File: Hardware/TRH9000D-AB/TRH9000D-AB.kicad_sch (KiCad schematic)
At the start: 22 parts, among them J5 DIN-8_SDF-80J, U4 74VHC138, U5 T.I_SN74LVC2G32DCTR, U8 LMH1980

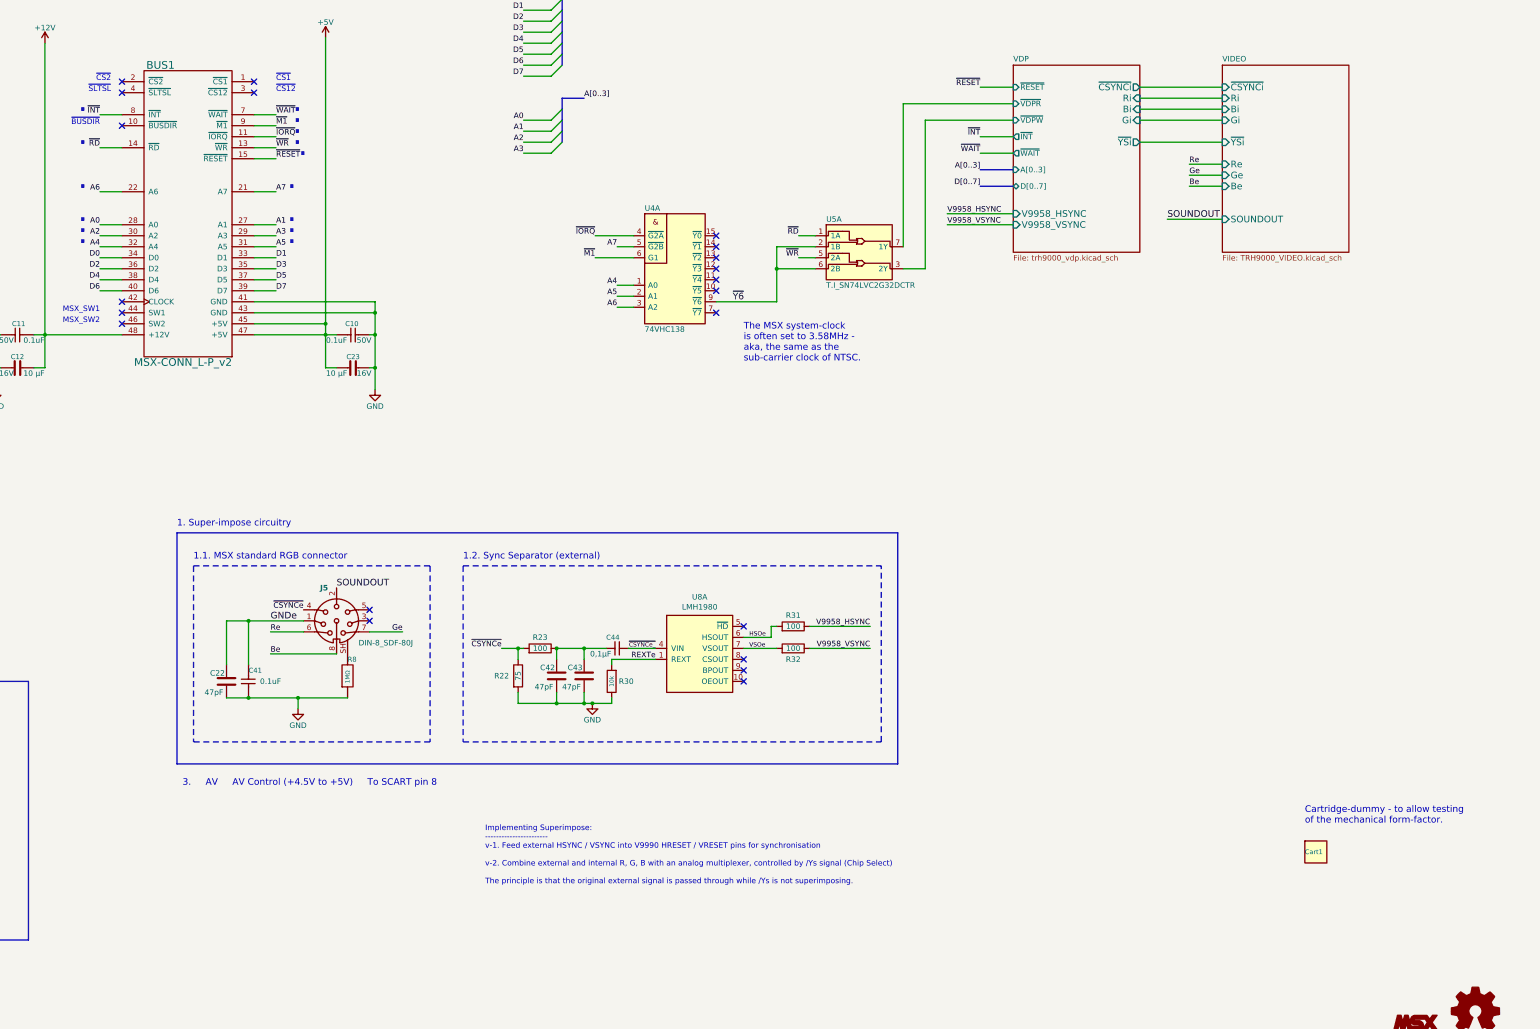
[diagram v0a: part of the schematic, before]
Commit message: Finished rerouting the AA-variant, and replaced the fuses with SMD-ones.
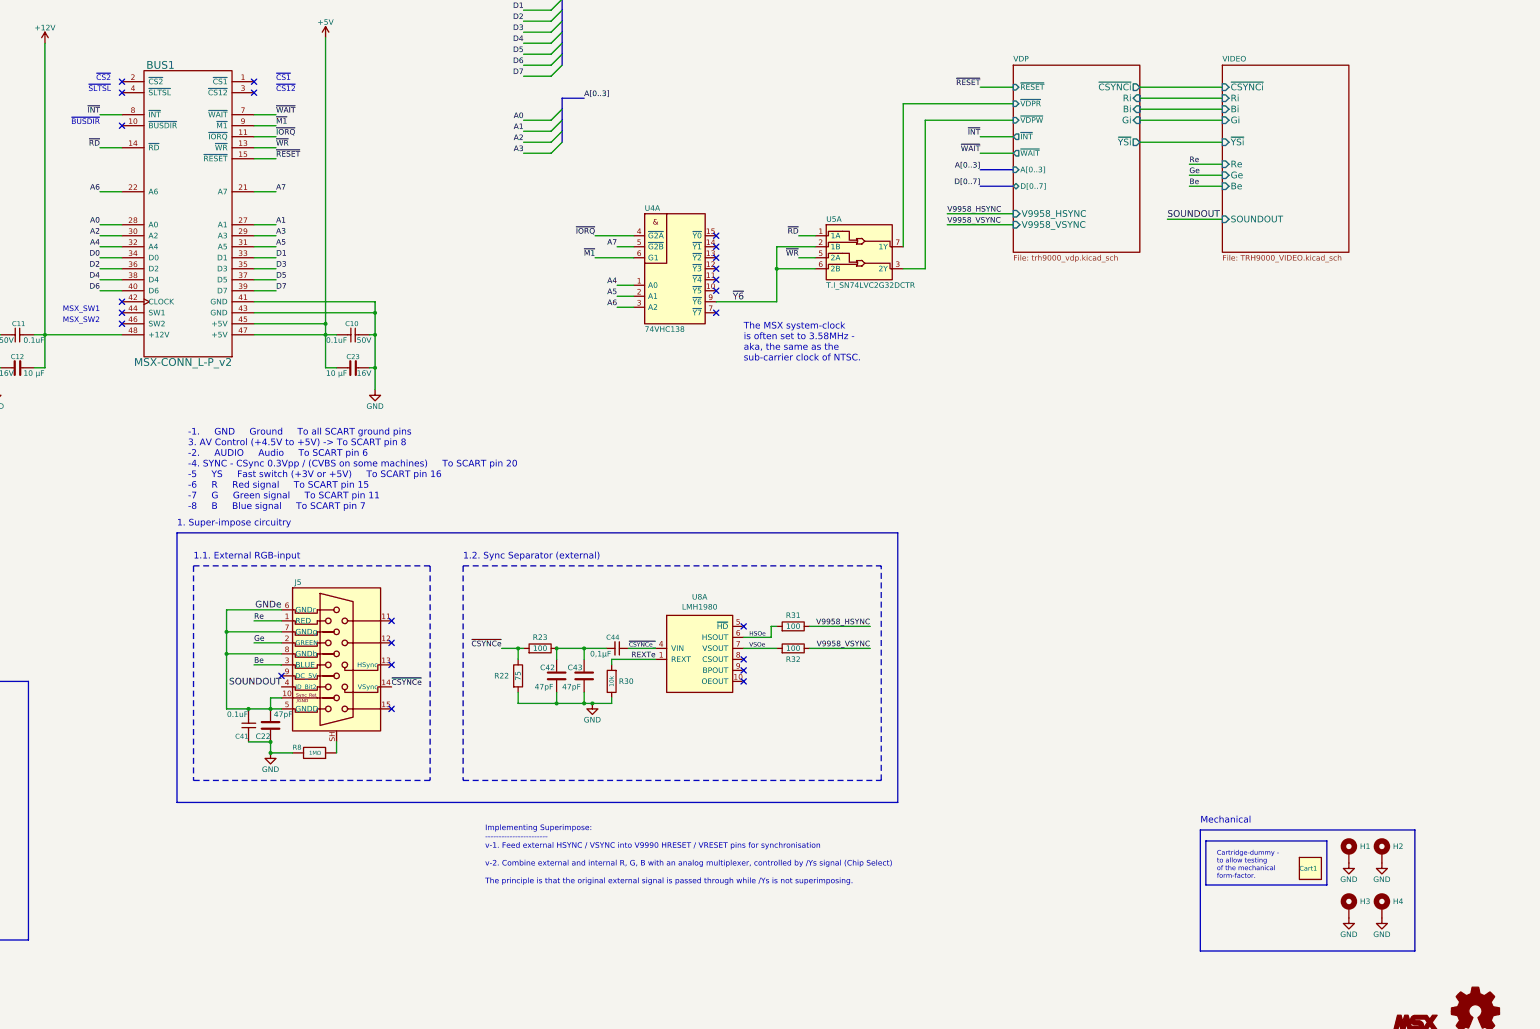
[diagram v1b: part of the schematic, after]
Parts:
- removed J5: DIN-8_SDF-80J, LRJ:Jack_DIN_CUI_SDF-80J_Horizontal, symbol LRJ-parts:DIN-8_SDF-80J
- added H1, H2, H3, H4: MountingHole_Pad, MountingHole:MountingHole_2.2mm_M2_ISO7380_Pad, symbol Mechanical:MountingHole_Pad
- added J5: Norcomp_200-015-263R001, LRJ:Norcomp_DSUB-15-HD_Female_Horizontal_SMD_P0.77x1.98mm, symbol LRJ-parts:Norcomp_200-015-263R001
- added LOGO2: Logo_MSX, Ultra-MSX:Logo_MSX_10x3, symbol Ultra-MSX:Logo_MSX
- LOGO1: now left out of the parts list
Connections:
- net Be: now also J5.3 (BLUE)
- net GND: now also C22.1, C41.1, R8.2, H1.1, H2.1, H3.1, H4.1; no longer C22.2, C41.2, R8.1
- net GNDe: now also C22.2, C41.2, J5.10 (Sync_Ret/GND), J5.5 (GNDD), J5.6 (GNDr), J5.7 (GNDg), J5.8 (GNDb); no longer C22.1, C41.1
- net Ge: now also J5.2 (GREEN)
- net Re: now also J5.1 (RED)
- net SOUNDOUT: now also J5.4 (ID_Bit2)
- net ~{CSYNCe}: now also J5.14 (VSync)
- new net: J5.SH, R8.1
- no-connect marks 21 -> 24
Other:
- note added: "-1. GND Ground To all SCART ground pins 3. AV Control (+4.5V to +5V) -> To SCART pin 8 -2. AUDIO Audio To SCART pin 6 -4. SYNC - CSync 0.3Vpp / (CVBS on some machines) To SCART pin 20 -5 YS Fast switch (+3V or +5V) To SCART pin 16 -6 R Red signal To SCART pin 15 -7 G Green signal To SCART pin 11 -8 B Blue signal To SCART pin 7"
- note added: "1.1. External RGB-input"
- note added: "Mechanical"
- note removed: "."
- note removed: "1.1. MSX standard RGB connector"
- note removed: "3. AV AV Control (+4.5V to +5V) To SCART pin 8"
- moved on the sheet: C22, C41, Cart1
